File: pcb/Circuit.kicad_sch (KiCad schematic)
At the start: 52 parts, among them J1 DTM13-12PA-R008, J2 TSW-101-07-T-D, J3 TSW-101-07-T-D, U1 MCP2561, U2 CDP68HC68S1, U3 LM2594HVM-5.0, U4 Teensy4.0

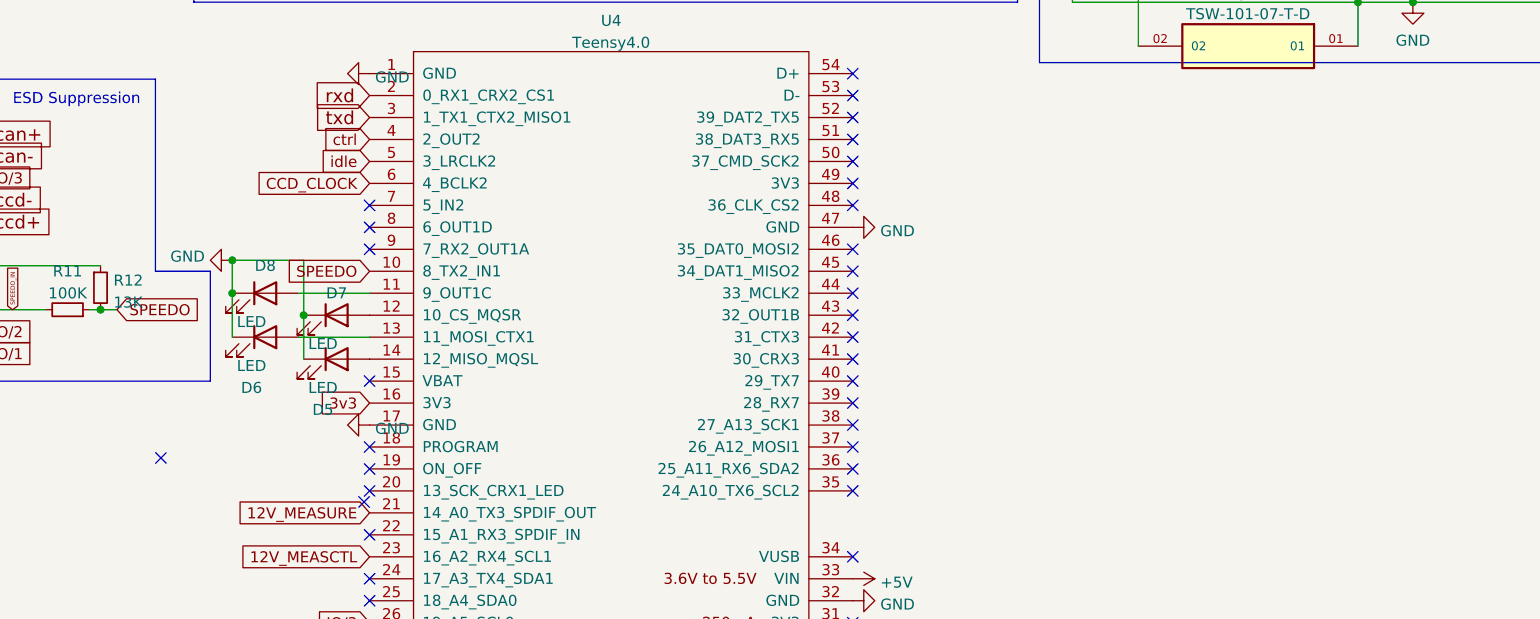
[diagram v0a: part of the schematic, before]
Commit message: Code for speedometer handling and odometer increment (not quite)
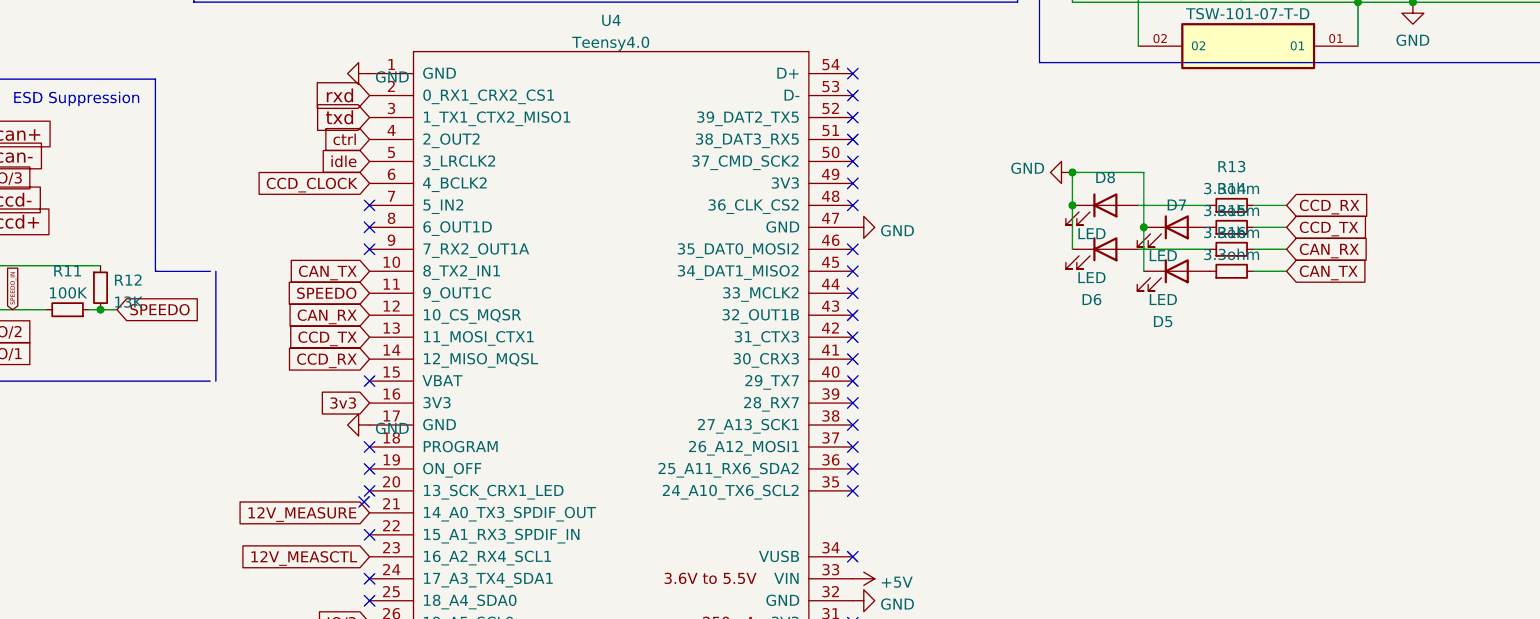
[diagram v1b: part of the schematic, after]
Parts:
- added R13, R14, R15, R16: 3.3ohm, Resistor_SMD:R_0603_1608Metric_Pad0.98x0.95mm_HandSolder, symbol Device:R_Small
- D5, D6, D7, D8: footprint LED_SMD:LED_0805_2012Metric -> LED_SMD:LED_0805_2012Metric_Pad1.15x1.40mm_HandSolder
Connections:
- net SPEEDO: now also U4.11 (9_OUT1C); no longer U4.10 (8_TX2_IN1)
- net at D8.2 (A): now also R13.1; no longer U4.11 (9_OUT1C)
- net at D6.2 (A): now also R15.1; no longer U4.13 (11_MOSI_CTX1)
- net at D7.2 (A): now also R14.1; no longer U4.12 (10_CS_MQSR)
- net at D5.2 (A): now also R16.1; no longer U4.14 (12_MISO_MQSL)
- new net CAN_RX: R15.2, U4.12 (10_CS_MQSR)
- new net CAN_TX: R16.2, U4.10 (8_TX2_IN1)
- new net CCD_RX: R13.2, U4.14 (12_MISO_MQSL)
- new net CCD_TX: R14.2, U4.13 (11_MOSI_CTX1)
- no-connect marks 36 -> 35
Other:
- moved on the sheet: D5, D6, D7, D8

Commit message: commit before changing can transceiver
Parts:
- removed D5, D6, D7, D8: LED, LED_SMD:LED_0805_2012Metric_Pad1.15x1.40mm_HandSolder, symbol Device:LED
- removed R13, R14, R15, R16: 3.3ohm, Resistor_SMD:R_0603_1608Metric_Pad0.98x0.95mm_HandSolder, symbol Device:R_Small
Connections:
- net 12V_MEASCTL: now also U4.22 (15_A1_RX3_SPDIF_IN); no longer U4.23 (16_A2_RX4_SCL1)
- net 3v3: now also U4.31 (3V3); no longer U4.16 (3V3)
- net CAN_RX: no longer names the net of U4.12 (10_CS_MQSR)
- net CAN_TX: no longer names the net of U4.10 (8_TX2_IN1)
- net CCD_RX: no longer names the net of U4.14 (12_MISO_MQSL)
- net CCD_TX: no longer names the net of U4.13 (11_MOSI_CTX1)
- no-connect marks 35 -> 38

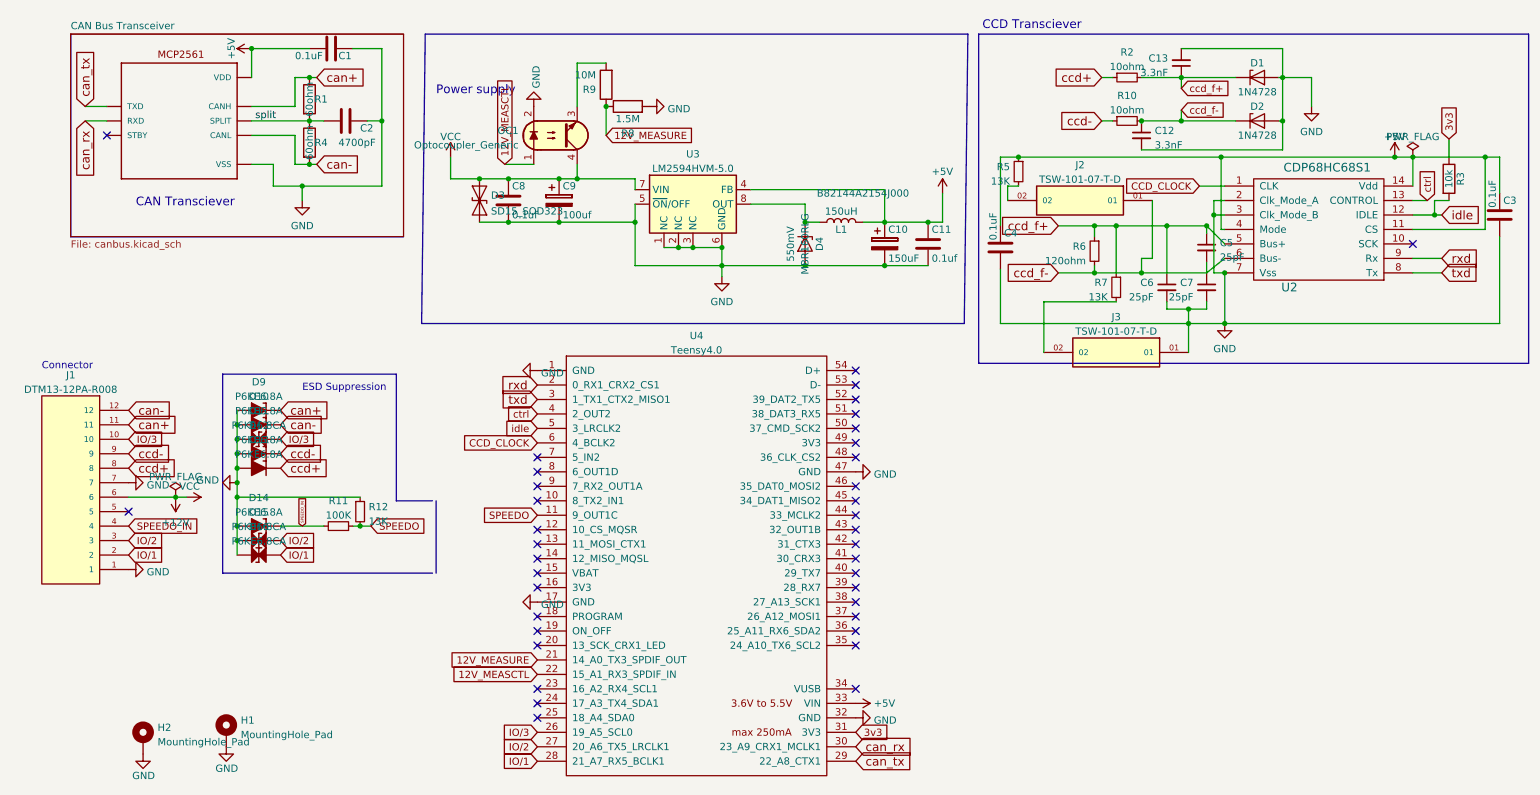
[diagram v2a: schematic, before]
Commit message: Move IO pins to more useful Teensy pins
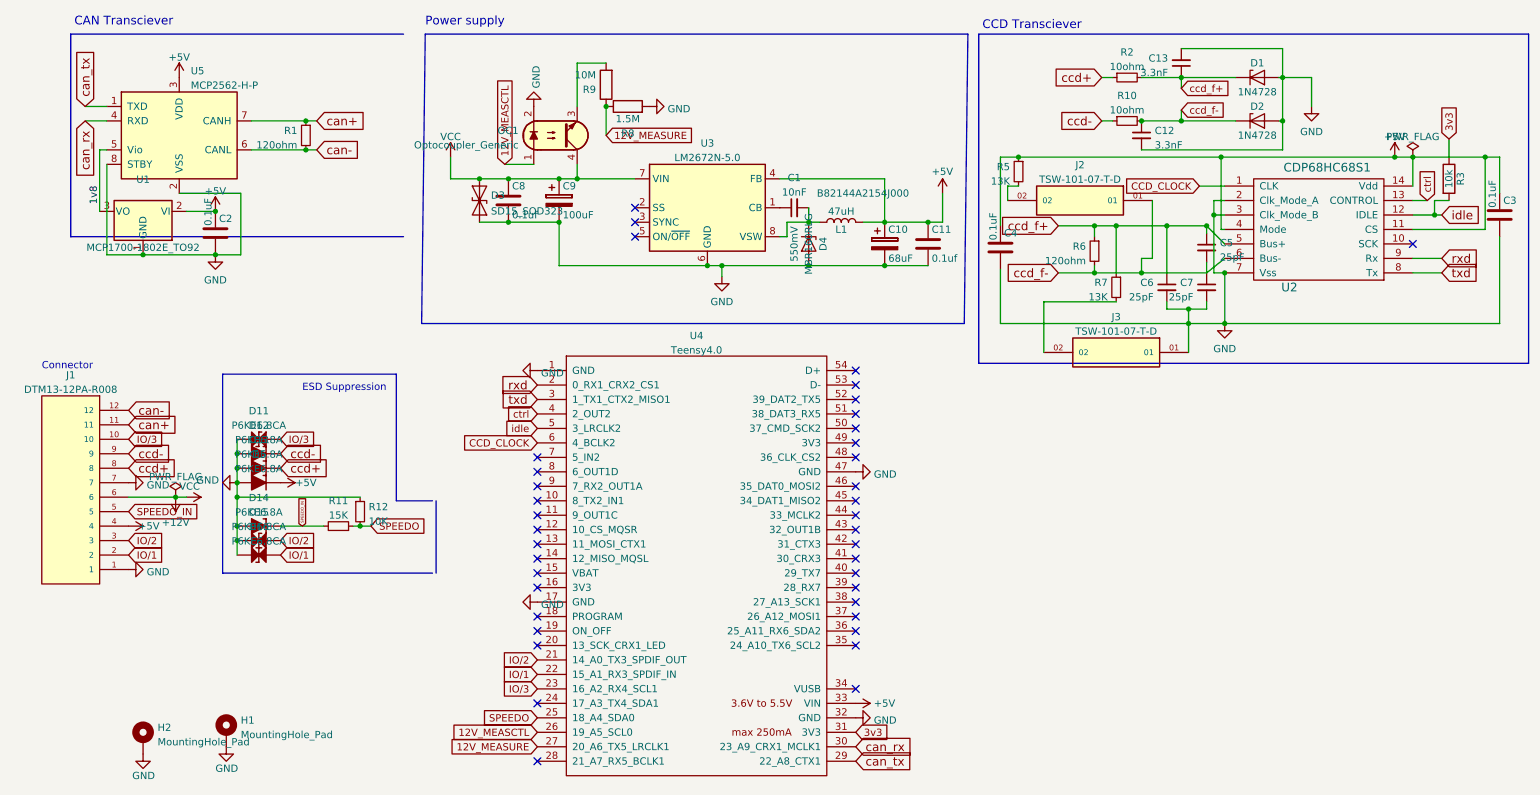
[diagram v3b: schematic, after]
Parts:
- removed C1: 0.1uF, Capacitor_THT:C_Disc_D7.0mm_W2.5mm_P5.00mm, symbol ccd_can_bridge-rescue:C
- removed D10, D9: P6KE6.8A, Diode_THT:D_DO-15_P10.16mm_Horizontal, symbol Diode_TVS_AKL:P6KE6.8A
- removed R1, R4: 60ohm, Resistor_THT:R_Axial_DIN0309_L9.0mm_D3.2mm_P12.70mm_Horizontal, symbol ccd_can_bridge-rescue:R
- removed U1: MCP2561, MCP2561:DIP787W46P254L927H533Q8, symbol ccd_can_bridge-rescue:MCP2561
- removed U3: LM2594HVM-5.0, Package_DIP:DIP-8_W7.62mm, symbol Regulator_Switching:LM2594HVM-5.0
- added C1: 10nF, Capacitor_THT:C_Radial_D5.0mm_H11.0mm_P2.00mm, symbol Device:C_Small
- added D5: P6KE6.8A, Diode_THT:D_DO-15_P10.16mm_Horizontal, symbol Diode_TVS_AKL:P6KE6.8A
- added R1: 120ohm, Resistor_THT:R_Axial_DIN0207_L6.3mm_D2.5mm_P7.62mm_Horizontal, symbol Device:R_Small
- added U1: MCP1700-1802E_TO92, Package_TO_SOT_THT:TO-92_Inline, symbol Regulator_Linear:MCP1700-1802E_TO92
- added U3: LM2672N-5.0, Package_DIP:DIP-8_W7.62mm, symbol Regulator_Switching:LM2672N-5.0
- added U5: MCP2562-H-P, Package_DIP:DIP-8_W7.62mm, symbol Interface_CAN_LIN:MCP2562-H-P
- C10: value 150uF -> 68uF; footprint Capacitor_THT:C_Disc_D7.0mm_W2.5mm_P5.00mm -> Capacitor_THT:C_Radial_D5.0mm_H11.0mm_P2.00mm
- C2: value 4700pF -> 0.1uF
- C9: value 100uf -> 100uF
- L1: value 150uH -> 47uH; footprint Inductor_THT:L_Axial_L12.0mm_D5.0mm_P15.24mm_Horizontal_Fastron_MISC -> Inductor_THT:L_Radial_D8.7mm_P5.00mm_Fastron_07HCP
- R11: value 100K -> 15K
- R12: value 13K -> 10K
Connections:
- net split is gone; now on net GND: C2.2
- net +12V: now also U3.7 (VIN)
- net +5V: now also C2.1, J1.4, D5.1 (K), U1.2 (VI), U3.4 (FB), U5.3 (VDD)
- net 12V_MEASCTL: now also U4.26 (19_A5_SCL0); no longer U4.22 (15_A1_RX3_SPDIF_IN)
- net 12V_MEASURE: now also U4.27 (20_A6_TX5_LRCLK1); no longer U4.21 (14_A0_TX3_SPDIF_OUT)
- net GND: now also D5.2 (A), U1.1 (GND), U3.6 (GND), U5.2 (VSS), U5.8 (STBY); no longer C2.1
- net IO/1: now also U4.22 (15_A1_RX3_SPDIF_IN); no longer U4.28 (21_A7_RX5_BCLK1)
- net IO/2: now also U4.21 (14_A0_TX3_SPDIF_OUT); no longer U4.27 (20_A6_TX5_LRCLK1)
- net IO/3: now also U4.23 (16_A2_RX4_SCL1); no longer U4.26 (19_A5_SCL0)
- net SPEEDO: now also U4.25 (18_A4_SDA0); no longer U4.11 (9_OUT1C)
- net SPEEDO_IN: now also J1.5; no longer J1.4
- net can+: now also R1.1, U5.7 (CANH)
- net can-: now also R1.2, U5.6 (CANL)
- net can_rx: now also U5.4 (RXD)
- net can_tx: now also U5.1 (TXD)
- net at D4.1 (K), L1.1: now also C1.2, U3.8 (VSW)
- new net: C1.1, U3.1 (CB)
- new net 1v8: U1.3 (VO), U5.5 (Vio)
- no-connect marks 38 -> 39
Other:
- removed sheet CAN Bus Transceiver
- moved on the sheet: D4

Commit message: linting
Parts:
- C5, C6, C7: footprint TSW-101:C_Disc_D6.5mm_W4mm_P6.4mm -> Capacitor_THT:C_Disc_D6.5mm_W4mm_P6.4mm
- J2, J3: footprint TSW-101:SAMTEC_TSW-101-07-T-D -> Jumpers:SAMTEC_TSW-101-07-T-D
- U2: footprint CDP68HC68S1:CDP68HC68S1 -> Transceivers:CDP68HC68S1
- U4: footprint Teensy 4.0:Teensy40_NoSMT -> MCUs:Teensy40_NoSMT
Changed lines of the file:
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@@
     (property "Reference" "U4" (id 0) (at 133.35 71.3572 0))
     (property "Value" "Teensy4.0" (id 1) (at 133.35 73.8941 0))
-    (property "Footprint" "Teensy 4.0:Teensy40_NoSMT" (id 2) (at 123.19 106.68 0)
+    (property "Footprint" "MCUs:Teensy40_NoSMT" (id 2) (at 123.19 106.68 0)
       (effects (font (size 1.27 1.27)) hide)
     )
@@
       (effects (font (size 1.27 1.27)) (justify left))
     )
-    (property "Footprint" "TSW-101:C_Disc_D6.5mm_W4mm_P6.4mm" (id 2) (at 215.9 62.865 0)
+    (property "Footprint" "Capacitor_THT:C_Disc_D6.5mm_W4mm_P6.4mm" (id 2) (at 215.9 62.865 0)
       (effects (font (size 1.27 1.27)) hide)
     )
@@
       (effects (font (size 1.524 1.524)))
     )
-    (property "Footprint" "CDP68HC68S1:CDP68HC68S1" (id 2) (at 244.0432 41.8338 0)
+    (property "Footprint" "Transceivers:CDP68HC68S1" (id 2) (at 244.0432 41.8338 0)
       (effects (font (size 1.524 1.524)) hide)
     )
@@
     (property "Reference" "J3" (id 0) (at 207.01 68.0552 0))
     (property "Value" "TSW-101-07-T-D" (id 1) (at 207.01 70.5921 0))
-    (property "Footprint" "TSW-101:SAMTEC_TSW-101-07-T-D" (id 2) (at 207.01 74.295 0)
+    (property "Footprint" "Jumpers:SAMTEC_TSW-101-07-T-D" (id 2) (at 207.01 74.295 0)
       (effects (font (size 1.27 1.27)) (justify left bottom) hide)
     )
@@
     (property "Reference" "J2" (id 0) (at 200.66 41.3852 0))
     (property "Value" "TSW-101-07-T-D" (id 1) (at 200.66 43.9221 0))
-    (property "Footprint" "TSW-101:SAMTEC_TSW-101-07-T-D" (id 2) (at 200.66 47.625 0)
+    (property "Footprint" "Jumpers:SAMTEC_TSW-101-07-T-D" (id 2) (at 200.66 47.625 0)
       (effects (font (size 1.27 1.27)) (justify left bottom) hide)
     )
@@
       (effects (font (size 1.27 1.27)) (justify right))
     )
-    (property "Footprint" "TSW-101:C_Disc_D6.5mm_W4mm_P6.4mm" (id 2) (at 222.885 55.88 0)
+    (property "Footprint" "Capacitor_THT:C_Disc_D6.5mm_W4mm_P6.4mm" (id 2) (at 222.885 55.88 0)
       (effects (font (size 1.27 1.27)) hide)
     )
@@
       (effects (font (size 1.27 1.27)) (justify left))
     )
-    (property "Footprint" "TSW-101:C_Disc_D6.5mm_W4mm_P6.4mm" (id 2) (at 222.885 62.865 0)
+    (property "Footprint" "Capacitor_THT:C_Disc_D6.5mm_W4mm_P6.4mm" (id 2) (at 222.885 62.865 0)
       (effects (font (size 1.27 1.27)) hide)
     )
@@
     )
     (path "/e2fe818b-e894-4111-8113-28ecb3a892a1"
-      (reference "C5") (unit 1) (value "25pF") (footprint "TSW-101:C_Disc_D6.5mm_W4mm_P6.4mm")
+      (reference "C5") (unit 1) (value "25pF") (footprint "Capacitor_THT:C_Disc_D6.5mm_W4mm_P6.4mm")
     )
     (path "/474365b3-872f-4e9f-9366-b68e0228856f"
-      (reference "C6") (unit 1) (value "25pF") (footprint "TSW-101:C_Disc_D6.5mm_W4mm_P6.4mm")
+      (reference "C6") (unit 1) (value "25pF") (footprint "Capacitor_THT:C_Disc_D6.5mm_W4mm_P6.4mm")
     )
     (path "/eb52f81a-44f2-4243-9ec4-d29bfe98c78d"
-      (reference "C7") (unit 1) (value "25pF") (footprint "TSW-101:C_Disc_D6.5mm_W4mm_P6.4mm")
+      (reference "C7") (unit 1) (value "25pF") (footprint "Capacitor_THT:C_Disc_D6.5mm_W4mm_P6.4mm")
     )
     (path "/5fa393d1-bc57-4048-a1c8-accb336b4802"
@@
     )
     (path "/df89e018-68cd-4312-b4c8-9dfbda41ae85"
-      (reference "J2") (unit 1) (value "TSW-101-07-T-D") (footprint "TSW-101:SAMTEC_TSW-101-07-T-D")
+      (reference "J2") (unit 1) (value "TSW-101-07-T-D") (footprint "Jumpers:SAMTEC_TSW-101-07-T-D")
     )
     (path "/9f4e2139-37ca-433c-9edc-8c5645d1e349"
-      (reference "J3") (unit 1) (value "TSW-101-07-T-D") (footprint "TSW-101:SAMTEC_TSW-101-07-T-D")
+      (reference "J3") (unit 1) (value "TSW-101-07-T-D") (footprint "Jumpers:SAMTEC_TSW-101-07-T-D")
     )
     (path "/0a29b72f-42cd-45ef-bfa3-6665ab368e8c"
@@
     )
     (path "/86884b69-c7b8-4118-8464-b297ee7a9704"
-      (reference "U2") (unit 1) (value "CDP68HC68S1") (footprint "CDP68HC68S1:CDP68HC68S1")
+      (reference "U2") (unit 1) (value "CDP68HC68S1") (footprint "Transceivers:CDP68HC68S1")
     )
     (path "/aaae18a7-7010-4c06-bdc3-efc8889ebd9e"
@@
     )
     (path "/133bb99a-82f3-4f77-a20b-451874ac44f4"
-      (reference "U4") (unit 1) (value "Teensy4.0") (footprint "Teensy 4.0:Teensy40_NoSMT")
+      (reference "U4") (unit 1) (value "Teensy4.0") (footprint "MCUs:Teensy40_NoSMT")
     )
     (path "/6ad50543-c10b-4e35-a9e8-1415ca733261"

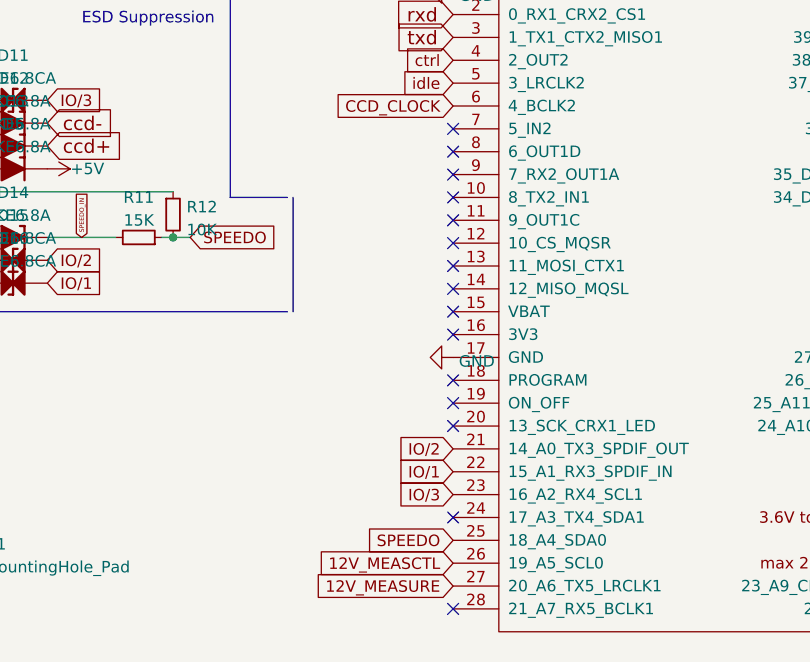
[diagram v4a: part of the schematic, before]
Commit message: Move speedo to a FlexPWM pin
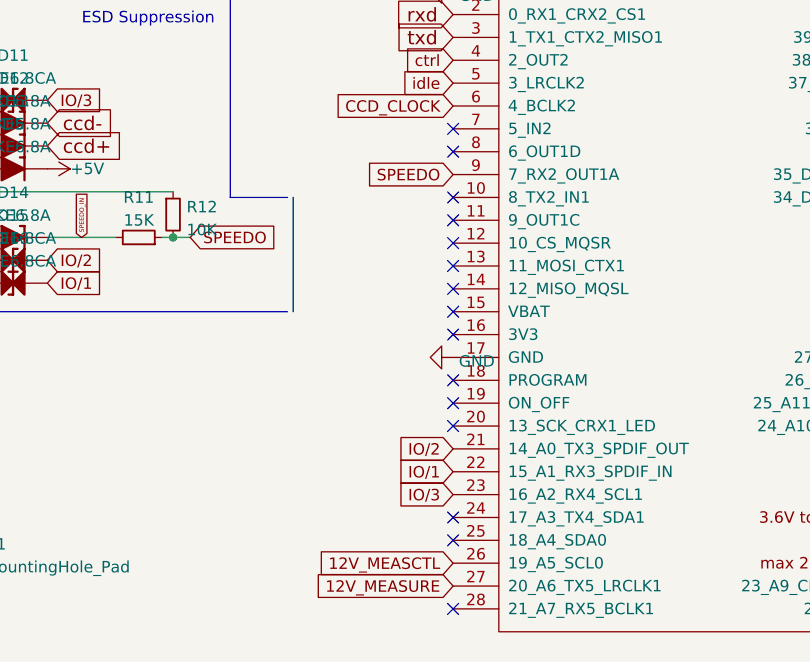
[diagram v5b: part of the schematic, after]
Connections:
- net SPEEDO: now also U4.9 (7_RX2_OUT1A); no longer U4.25 (18_A4_SDA0)
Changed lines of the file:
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@@
   (no_connect (at 161.29 85.09))
   (no_connect (at 161.29 82.55))
-  (no_connect (at 105.41 97.79))
+  (no_connect (at 105.41 138.43))
   (no_connect (at 105.41 105.41))
   (no_connect (at 105.41 135.89))
@@
     )
   )
-  (global_label "SPEEDO" (shape input) (at 105.41 138.43 180) (fields_autoplaced)
+  (global_label "SPEEDO" (shape input) (at 105.41 97.79 180) (fields_autoplaced)
     (effects (font (size 1.27 1.27)) (justify right))
-    (property "Intersheet References" "${INTERSHEET_REFS}" (id 0) (at 95.6188 138.5094 0)
+    (property "Intersheet References" "${INTERSHEET_REFS}" (id 0) (at 95.6188 97.8694 0)
       (effects (font (size 1.27 1.27)) (justify right) hide)
     )
